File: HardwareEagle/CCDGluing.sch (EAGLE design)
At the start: 7 parts, among them X1 BU-SMA-G

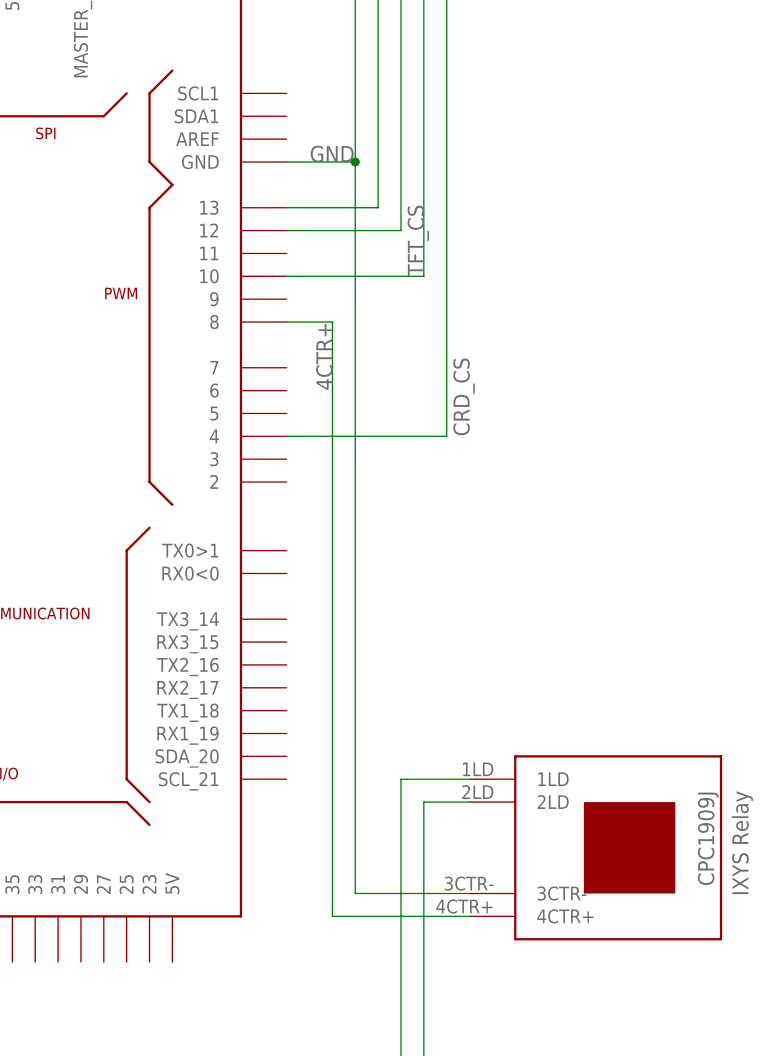
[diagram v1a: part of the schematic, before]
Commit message: Added current limit resistor.
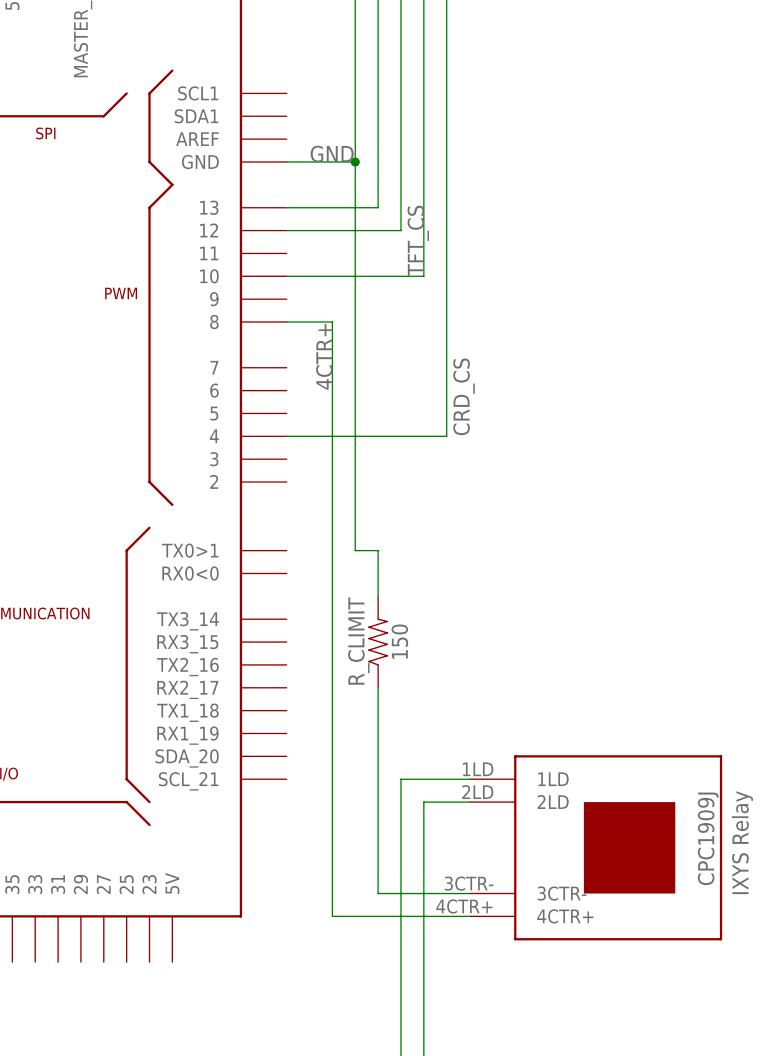
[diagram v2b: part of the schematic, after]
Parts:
- added R_CLIMIT: 150, SparkFun-Resistors:150OHM-0603-1/10W-1%
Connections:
- new net N$1: K1.3CTR-, R_CLIMIT.1
- net GND: now also R_CLIMIT.2; no longer K1.3CTR-
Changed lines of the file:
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@@
 <part name="LCDCONN" library="SparkFun-Connectors" library_urn="urn:adsk.eagle:library:513" deviceset="CONN_10" device="&quot;" package3d_urn="urn:adsk.eagle:package:38157/1" value="ST7735R_cnn"/>
 <part name="LOADOUT" library="Wurth_Elektronik_Electromechanic_DC_Power_Jack_Connectors_rev18b" library_urn="urn:adsk.eagle:library:438" deviceset="694103107102" device="" package3d_urn="urn:adsk.eagle:package:3359601/1"/>
+<part name="R_CLIMIT" library="SparkFun-Resistors" library_urn="urn:adsk.eagle:library:532" deviceset="150OHM" device="-0603-1/10W-1%" package3d_urn="urn:adsk.eagle:package:39650/1" value="150"/>
 </parts>
 <sheets>
@@
 <attribute name="NAME" x="170.18" y="-45.72" size="1.778" layer="95" rot="R180"/>
 <attribute name="VALUE" x="170.18" y="-35.56" size="1.778" layer="96" rot="R180"/>
+</instance>
+<instance part="R_CLIMIT" gate="G$1" x="139.7" y="20.32" smashed="yes" rot="R90">
+<attribute name="NAME" x="138.176" y="20.32" size="1.778" layer="95" font="vector" rot="R90" align="bottom-center"/>
+<attribute name="VALUE" x="141.224" y="20.32" size="1.778" layer="96" font="vector" rot="R90" align="top-center"/>
 </instance>
 </instances>
@@
 <pinref part="LCDCONN" gate="G$1" pin="10"/>
 <wire x1="83.82" y1="127" x2="137.16" y2="127" width="0.1524" layer="91"/>
-<pinref part="K1" gate="G$1" pin="3CTR-"/>
 <pinref part="ARDUINO_DUE1" gate="G$1" pin="GND@4"/>
-<wire x1="149.86" y1="-7.62" x2="137.16" y2="-7.62" width="0.1524" layer="91"/>
-<wire x1="137.16" y1="-7.62" x2="137.16" y2="73.66" width="0.1524" layer="91"/>
 <wire x1="137.16" y1="73.66" x2="129.54" y2="73.66" width="0.1524" layer="91"/>
 <label x="132.08" y="73.66" size="1.778" layer="95"/>
 <wire x1="137.16" y1="127" x2="137.16" y2="73.66" width="0.1524" layer="91"/>
+<wire x1="137.16" y1="73.66" x2="137.16" y2="30.48" width="0.1524" layer="91"/>
 <junction x="137.16" y="73.66"/>
+<wire x1="137.16" y1="30.48" x2="139.7" y2="30.48" width="0.1524" layer="91"/>
+<pinref part="R_CLIMIT" gate="G$1" pin="2"/>
+<wire x1="139.7" y1="30.48" x2="139.7" y2="25.4" width="0.1524" layer="91"/>
 </segment>
 </net>
@@
 </segment>
 </net>
+<net name="N$1" class="0">
+<segment>
+<pinref part="K1" gate="G$1" pin="3CTR-"/>
+<wire x1="149.86" y1="-7.62" x2="139.7" y2="-7.62" width="0.1524" layer="91"/>
+<pinref part="R_CLIMIT" gate="G$1" pin="1"/>
+<wire x1="139.7" y1="-7.62" x2="139.7" y2="15.24" width="0.1524" layer="91"/>
+</segment>
+</net>
